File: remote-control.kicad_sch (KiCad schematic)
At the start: 2 parts, among them J1 Conn_01x05_Pin, U1 ESP32S3WROOM1N8R8

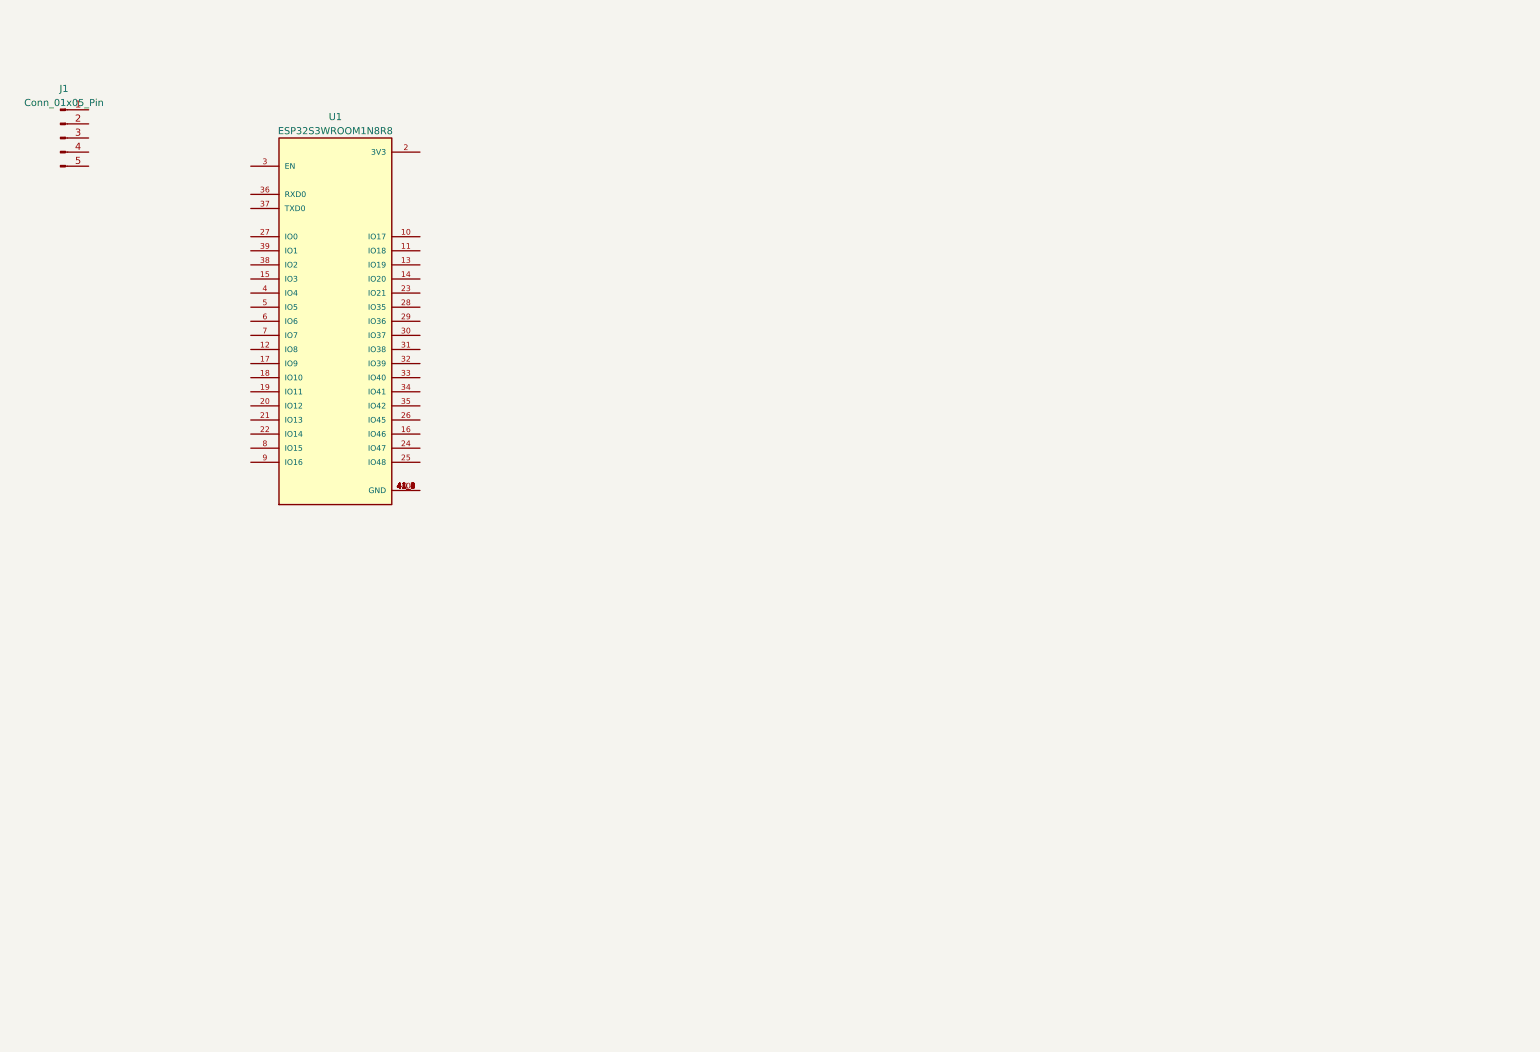
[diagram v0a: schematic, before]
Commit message: Replicated flux schematic
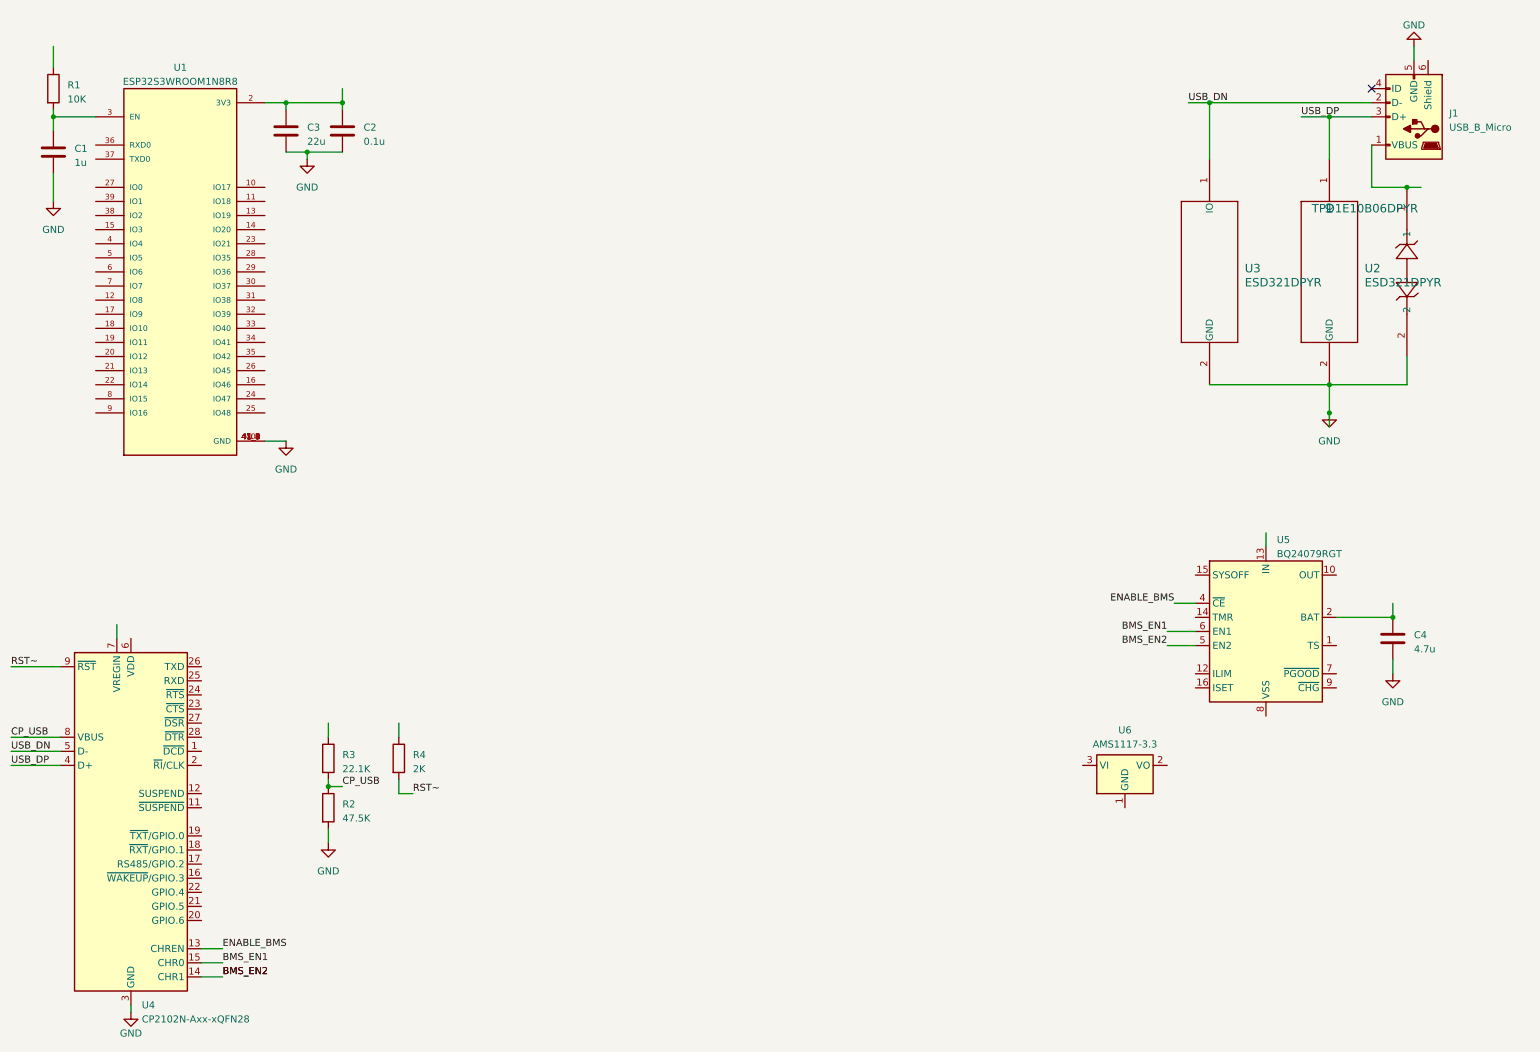
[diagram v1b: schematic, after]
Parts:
- removed J1: Conn_01x05_Pin, symbol Connector:Conn_01x05_Pin
- added 1: TPD1E10B06DPYR, symbol 2023-07-28_15-11-32:TPD1E10B06DPYR
- added C1: 1u, symbol Device:C
- added C2: 0.1u, symbol Device:C
- added C3: 22u, symbol Device:C
- added C4: 4.7u, symbol Device:C
- added J1: USB_B_Micro, symbol Connector:USB_B_Micro
- added R1: 10K, symbol Device:R
- added R2: 47.5K, symbol Device:R
- added R3: 22.1K, symbol Device:R
- added R4: 2K, symbol Device:R
- added U2, U3: ESD321DPYR, DPY2_TEX, symbol 2023-07-27_21-37-44:ESD321DPYR
- added U4: CP2102N-Axx-xQFN28, Package_DFN_QFN:QFN-28-1EP_5x5mm_P0.5mm_EP3.35x3.35mm, symbol Interface_USB:CP2102N-Axx-xQFN28
- added U5: BQ24079RGT, Package_DFN_QFN:VQFN-16-1EP_3x3mm_P0.5mm_EP1.6x1.6mm, symbol Battery_Management:BQ24079RGT
- added U6: AMS1117-3.3, Package_TO_SOT_SMD:SOT-223-3_TabPin2, symbol Regulator_Linear:AMS1117-3.3
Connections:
- net GND: now reaches U1.1 (GND), U1.40 (GND), U1.41_1 (GND), U1.41_2 (GND), U1.41_3 (GND), U1.41_4 (GND), U1.41_5 (GND), U1.41_6 (GND), U1.41_7 (GND), U1.41_8 (GND), U1.41_9 (GND)
- net GND: now also 1.2, C1.2, C2.2, C3.2, C4.2, J1.5 (GND), R2.2, U2.2 (GND), U3.2 (GND), U4.29 (GND), U4.3 (GND)
- net at U1.2 (3V3): now also C2.1, C3.1
- net at U1.3 (EN): now also C1.1, R1.2
- new net: U5.10 (OUT), U5.11 (OUT)
- new net: U5.17 (VSS), U5.8 (VSS)
- new net: C4.1, U5.2 (BAT), U5.3 (BAT)
- new net: 1.1, J1.1 (VBUS)
- new net BMS_EN1: U4.15 (CHR0), U5.6 (EN1)
- new net BMS_EN2: U4.14 (CHR1), U5.5 (EN2)
- new net CP_USB: R2.1, R3.2, U4.8 (VBUS)
- new net ENABLE_BMS: U4.13 (CHREN), U5.4 (~{CE})
- new net RST~: R4.2, U4.9 (~{RST})
- new net USB_DN: J1.2 (D-), U3.1 (IO), U4.5 (D-)
- new net USB_DP: J1.3 (D+), U2.1 (IO), U4.4 (D+)
- no-connect marks 0 -> 1
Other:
- moved on the sheet: U1

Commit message: Add STV7799V interface
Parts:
- added J2: Conn_01x08_Pin, symbol Connector:Conn_01x08_Pin
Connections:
- net GND: now also J2.2 (Pin_2)
- new net 3V3: J2.1 (Pin_1)
- new net MOSI: J2.3 (Pin_3)
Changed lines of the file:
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@@
+    (stroke (width 0) (type default))
+  )
+  (wire (pts (xy 88.9 25.4) (xy 102.87 25.4))
     (stroke (width 0) (type default))
   )
@@
     (stroke (width 0) (type default))
   )
+  (wire (pts (xy 88.9 27.94) (xy 92.71 27.94))
+    (stroke (width 0) (type default))
+  )
   (wire (pts (xy 257.81 29.21) (xy 228.6 29.21))
     (stroke (width 0) (type default))
@@
   )
   (wire (pts (xy 257.81 44.45) (xy 264.16 44.45))
+    (stroke (width 0) (type default))
+  )
+  (wire (pts (xy 88.9 22.86) (xy 92.71 22.86))
     (stroke (width 0) (type default))
   )
@@
     (effects (font (size 1.27 1.27)) (justify left bottom))
   )
+  (label "MOSI" (at 92.71 27.94 0) (fields_autoplaced)
+    (effects (font (size 1.27 1.27)) (justify left bottom))
+  )
   (label "USB_DP" (at 12.7 148.59 0) (fields_autoplaced)
     (effects (font (size 1.27 1.27)) (justify left bottom))
@@
   )
   (label "USB_DP" (at 245.11 31.75 0) (fields_autoplaced)
+    (effects (font (size 1.27 1.27)) (justify left bottom))
+  )
+  (label "3V3" (at 92.71 22.86 0) (fields_autoplaced)
     (effects (font (size 1.27 1.27)) (justify left bottom))
   )
@@
     (effects (font (size 1.27 1.27)) (justify right bottom))
   )
+  (label "CLK" (at 92.71 30.48 0) (fields_autoplaced)
+    (effects (font (size 1.27 1.27)) (justify left bottom))
+  )
   (label "BMS_EN2" (at 50.8 186.69 0) (fields_autoplaced)
     (effects (font (size 1.27 1.27)) (justify left bottom))
@@
   )
   (label "USB_DN" (at 12.7 146.05 0) (fields_autoplaced)
+    (effects (font (size 1.27 1.27)) (justify left bottom))
+  )
+  (label "CS_LCD" (at 92.71 33.02 0) (fields_autoplaced)
     (effects (font (size 1.27 1.27)) (justify left bottom))
   )
@@
     )
   )
+  (symbol (lib_id "Connector:Conn_01x08_Pin") (at 83.82 30.48 0) (unit 1)
+    (in_bom yes) (on_board yes) (dnp no) (fields_autoplaced)
+    (property "Reference" "J2" (at 84.455 19.05 0)
+      (effects (font (size 1.27 1.27)))
+    )
+    (property "Value" "Conn_01x08_Pin" (at 84.455 21.59 0)
+      (effects (font (size 1.27 1.27)))
+    )
+    (property "Footprint" "" (at 83.82 30.48 0)
+      (effects (font (size 1.27 1.27)) hide)
+    )
+    (property "Datasheet" "~" (at 83.82 30.48 0)
+      (effects (font (size 1.27 1.27)) hide)
+    )
+    (pin "1")
+    (pin "2")
+    (pin "3")
+    (pin "4")
+    (pin "5")
+    (pin "6")
+    (pin "7")
+    (pin "8")
+    (instances
+      (project "remote-control"
+        (path "/0c7d532e-7a5c-43b5-bbb8-19411d161f3b"
+          (reference "J2") (unit 1)
+        )
+      )
+    )
+  )
   (symbol (lib_id "Device:R") (at 69.85 156.21 0) (unit 1)
     (in_bom yes) (on_board yes) (dnp no) (fields_autoplaced)
@@
         )
       )
+    )
+  )
+  (symbol (lib_id "power:GND") (at 102.87 25.4 0) (unit 1)
+    (in_bom yes) (on_board yes) (dnp no) (fields_autoplaced)
+    (property "Reference" "#PWR09" (at 102.87 31.75 0)
+      (effects (font (size 1.27 1.27)) hide)
+    )
+    (property "Value" "GND" (at 102.87 30.48 0)
+      (effects (font (size 1.27 1.27)))
+    )
+    (property "Footprint" "" (at 102.87 25.4 0)
+      (effects (font (size 1.27 1.27)) hide)
+    )
+    (property "Datasheet" "" (at 102.87 25.4 0)
+      (effects (font (size 1.27 1.27)) hide)
+    )
+    (pin "1")
+    (instances
+      (project "remote-control"
+        (path "/0c7d532e-7a5c-43b5-bbb8-19411d161f3b"
+          (reference "#PWR09") (unit 1)
+        )
+      )

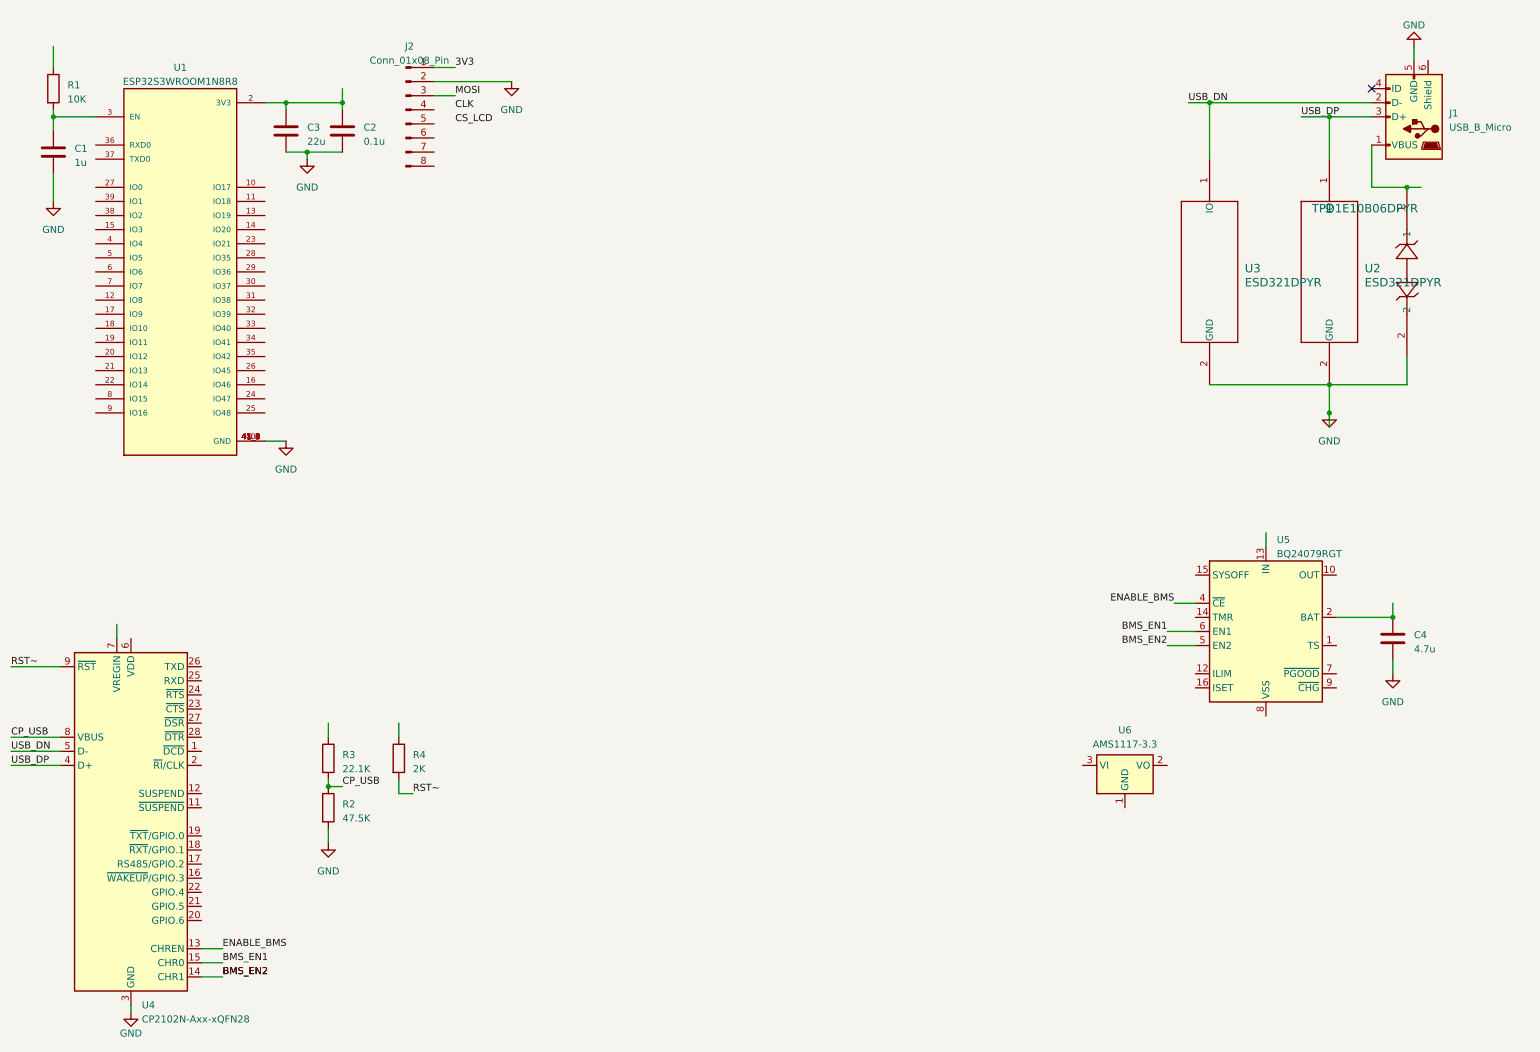
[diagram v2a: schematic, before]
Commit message: Add STV7799V interface
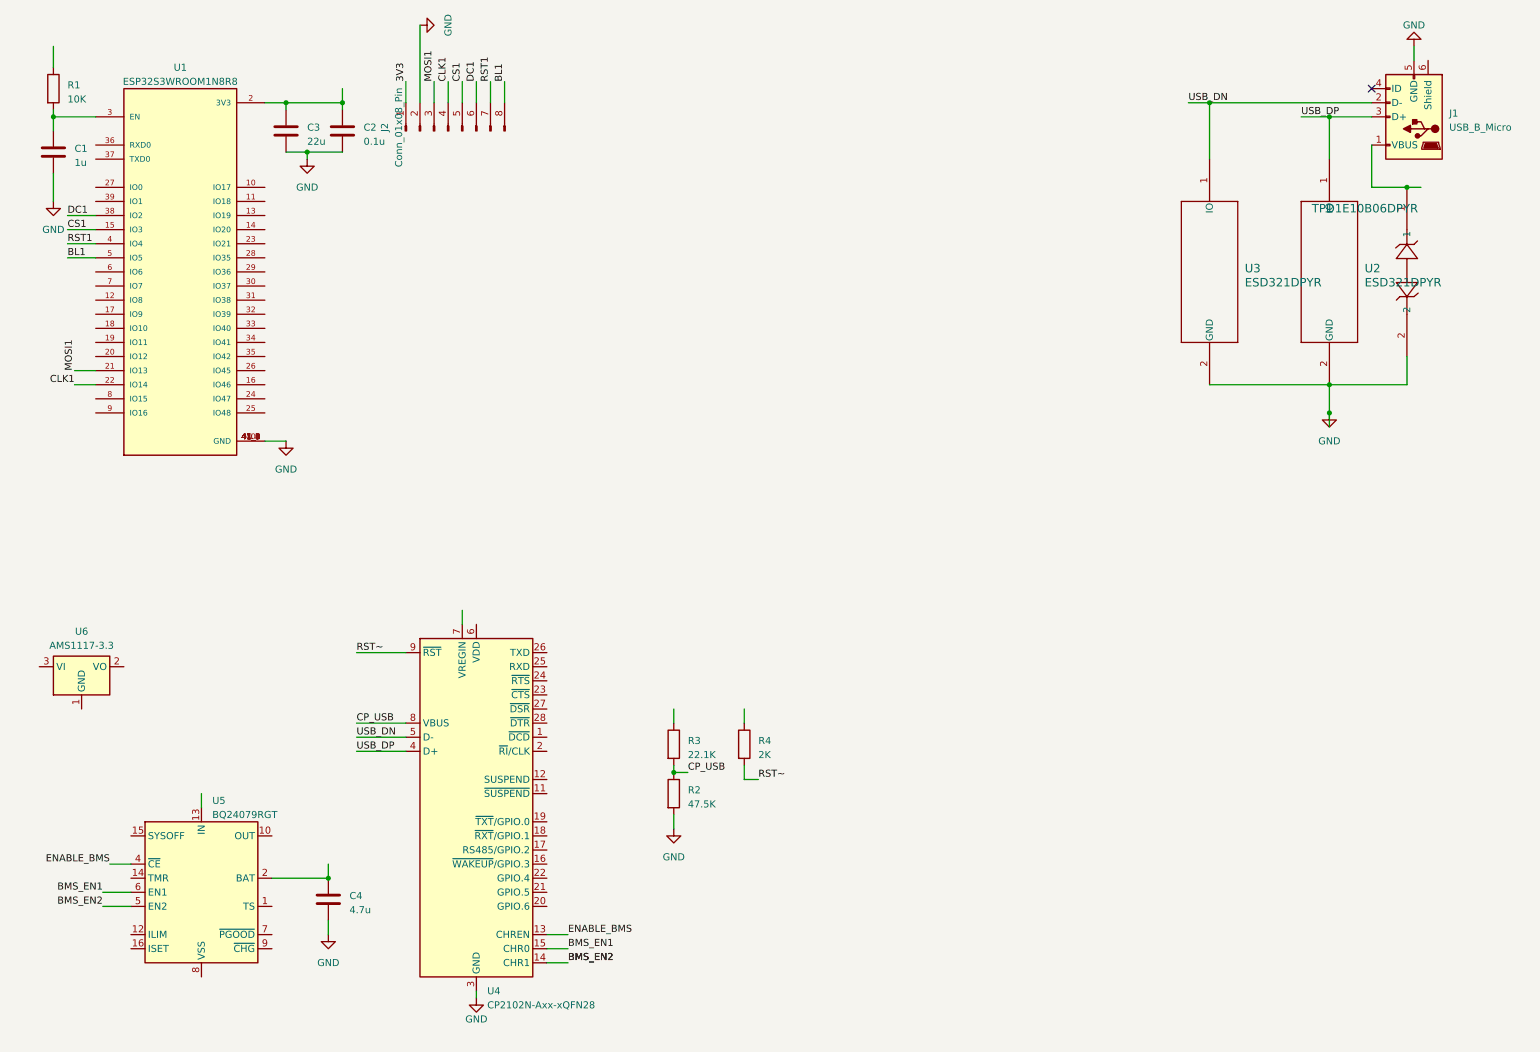
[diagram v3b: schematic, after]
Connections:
- net MOSI is gone; now on net MOSI1: J2.3 (Pin_3)
- net CLK1: now reaches J2.4 (Pin_4)
- net CLK1: now also U1.22 (IO14)
- net CS1: now reaches J2.5 (Pin_5)
- net CS1: now also U1.15 (IO3)
- net DC1: now reaches J2.6 (Pin_6)
- net DC1: now also U1.38 (IO2)
- net RST1: now reaches J2.7 (Pin_7)
- net RST1: now also U1.4 (IO4)
- net BL1: now reaches J2.8 (Pin_8)
- net BL1: now also U1.5 (IO5)
- net MOSI1: now reaches U1.21 (IO13)
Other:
- moved on the sheet: C4, J2, R2, R3, R4, U4, U5, U6
